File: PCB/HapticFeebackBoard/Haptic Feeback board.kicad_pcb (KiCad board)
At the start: 2 copper layers, 43.5 x 37.5 mm, 12 parts, among them J1 1769, J2 Conn_01x02, M1 Conn_01x02, M2 Conn_01x02, Q1 2N7002E, SW1 PTS526 SM15 SMTR2 LFS

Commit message: Generated Gerber Files
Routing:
- net Net-(C1-Pad1): track 6.64 -> 10.3 mm
- net GND: vias 3 -> 4
- added copper zone on B.Cu, net GND
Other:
- board size 43.5 x 37.5 mm -> 46 x 41 mm
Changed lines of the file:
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@@
 			(disableapertmacros no)
 			(usegerberextensions no)
-			(usegerberattributes yes)
+			(usegerberattributes no)
 			(usegerberadvancedattributes yes)
 			(creategerberjobfile yes)
@@
 			(outputformat 1)
 			(mirror no)
-			(drillshape 1)
+			(drillshape 0)
 			(scaleselection 1)
 			(outputdirectory "")
@@
 			(size 1.175 1.45)
 			(layers "F.Cu" "F.Paste" "F.Mask")
-			(roundrect_rratio 0.212766)
+			(roundrect_rratio 0.2127659574)
 			(net 1 "Net-(C1-Pad1)")
 			(pintype "passive")
@@
 			(size 1.175 1.45)
 			(layers "F.Cu" "F.Paste" "F.Mask")
-			(roundrect_rratio 0.212766)
+			(roundrect_rratio 0.2127659574)
 			(net 2 "GND")
 			(pintype "passive")
@@
 			(layers "*.Cu" "*.Mask")
 			(remove_unused_layers no)
-			(roundrect_rratio 0.143678)
+			(roundrect_rratio 0.1436781609)
 			(net 6 "/MCU")
 			(pinfunction "Pin_1")
@@
 			(layers "*.Cu" "*.Mask")
 			(remove_unused_layers no)
-			(roundrect_rratio 0.143678)
+			(roundrect_rratio 0.1436781609)
 			(net 5 "/Motor1")
 			(pinfunction "Pin_1")
@@
 			(layers "*.Cu" "*.Mask")
 			(remove_unused_layers no)
-			(roundrect_rratio 0.143678)
+			(roundrect_rratio 0.1436781609)
 			(net 5 "/Motor1")
 			(pinfunction "Pin_1")
@@
 			(size 1.2 1.4)
 			(layers "F.Cu" "F.Paste" "F.Mask")
-			(roundrect_rratio 0.208333)
+			(roundrect_rratio 0.2083333333)
 			(net 1 "Net-(C1-Pad1)")
 			(pintype "passive")
@@
 			(size 1.2 1.4)
 			(layers "F.Cu" "F.Paste" "F.Mask")
-			(roundrect_rratio 0.208333)
+			(roundrect_rratio 0.2083333333)
 			(net 6 "/MCU")
 			(pintype "passive")
@@
 	)
 	(gr_rect
-		(start 119.5 78.5)
-		(end 163 116)
+		(start 118.5 77)
+		(end 164.5 118)
 		(stroke
 			(width 0.1)
@@
 		(layer "Edge.Cuts")
 	)
-	(dimension
-		(type aligned)
-		(layer "F.Cu")
-		(pts
-			(xy 156.5 112) (xy 156.5 83)
-		)
-		(height 12.5)
-		(gr_text "29.0000 mm"
-			(at 167.2 97.5 90)
-			(layer "F.Cu")
-			(effects
-				(font
-					(size 1.5 1.5)
-					(thickness 0.3)
-				)
-			)
-		)
-		(format
-			(prefix "")
-			(suffix "")
-			(units 3)
-			(units_format 1)
-			(precision 4)
-		)
-		(style
-			(thickness 0.2)
-			(arrow_length 1.27)
-			(text_position_mode 0)
-			(extension_height 0.58642)
-			(extension_offset 0.5) keep_text_aligned)
-	)
-	(dimension
-		(type aligned)
+	(segment
+		(start 134.239 96.3676)
+		(end 135.9447 96.3676)
+		(width 0.254)
 		(layer "F.Cu")
-		(pts
-			(xy 156.5 112) (xy 125.5 112)
-		)
-		(height -9)
-		(gr_text "31.0000 mm"
-			(at 141 119.2 0)
-			(layer "F.Cu")
-			(effects
-				(font
-					(size 1.5 1.5)
-					(thickness 0.3)
-				)
-			)
-		)
-		(format
-			(prefix "")
-			(suffix "")
-			(units 3)
-			(units_format 1)
-			(precision 4)
-		)
-		(style
-			(thickness 0.2)
-			(arrow_length 1.27)
-			(text_position_mode 0)
-			(extension_height 0.58642)
-			(extension_offset 0.5) keep_text_aligned)
+		(net 1)
 	)
 	(segment
 		(start 134.239 96.3676)
-		(end 135.9447 96.3676)
+		(end 134.239 92.667602)
 		(width 0.254)
 		(layer "F.Cu")
@@
 	)
 	(via
-		(at 152.5 90)
+		(at 132.5 88)
+		(size 0.8)
+		(drill 0.4)
+		(layers "F.Cu" "B.Cu")
+		(free yes)
+		(net 2)
+	)
+	(via
+		(at 140.5 107.5)
 		(size 0.8)
 		(drill 0.4)
@@
 	)
 	(via
-		(at 141 108)
+		(at 141 95)
 		(size 0.8)
 		(drill 0.4)
@@
 	)
 	(via
-		(at 131.5 88)
+		(at 152 88)
 		(size 0.8)
 		(drill 0.4)
@@
 			)
 		)
+	)
+	(zone
+		(net 2)
+		(net_name "GND")
+		(layer "B.Cu")
+		(hatch edge 0.5)
+		(priority 1)
+		(connect_pads
+			(clearance 0.5)
+		)
+		(min_thickness 0.25)
+		(filled_areas_thickness no)
+		(fill yes
+			(thermal_gap 0.5)
+			(thermal_bridge_width 0.5)
+		)
+		(polygon
+			(pts
+				(xy 93.5 70) (xy 175.5 70) (xy 176 130.5) (xy 93.5 130)
+			)
+		)

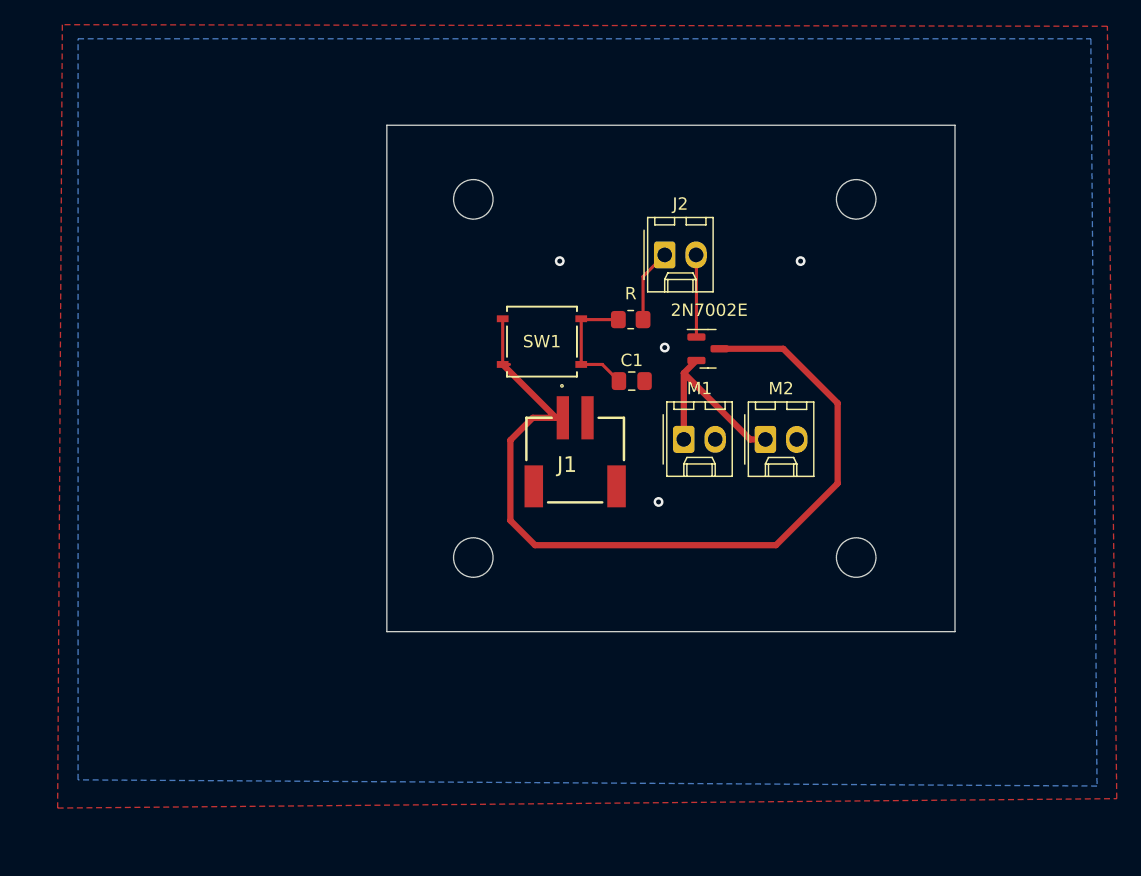
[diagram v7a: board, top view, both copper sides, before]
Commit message: Minor copper pour adjustments
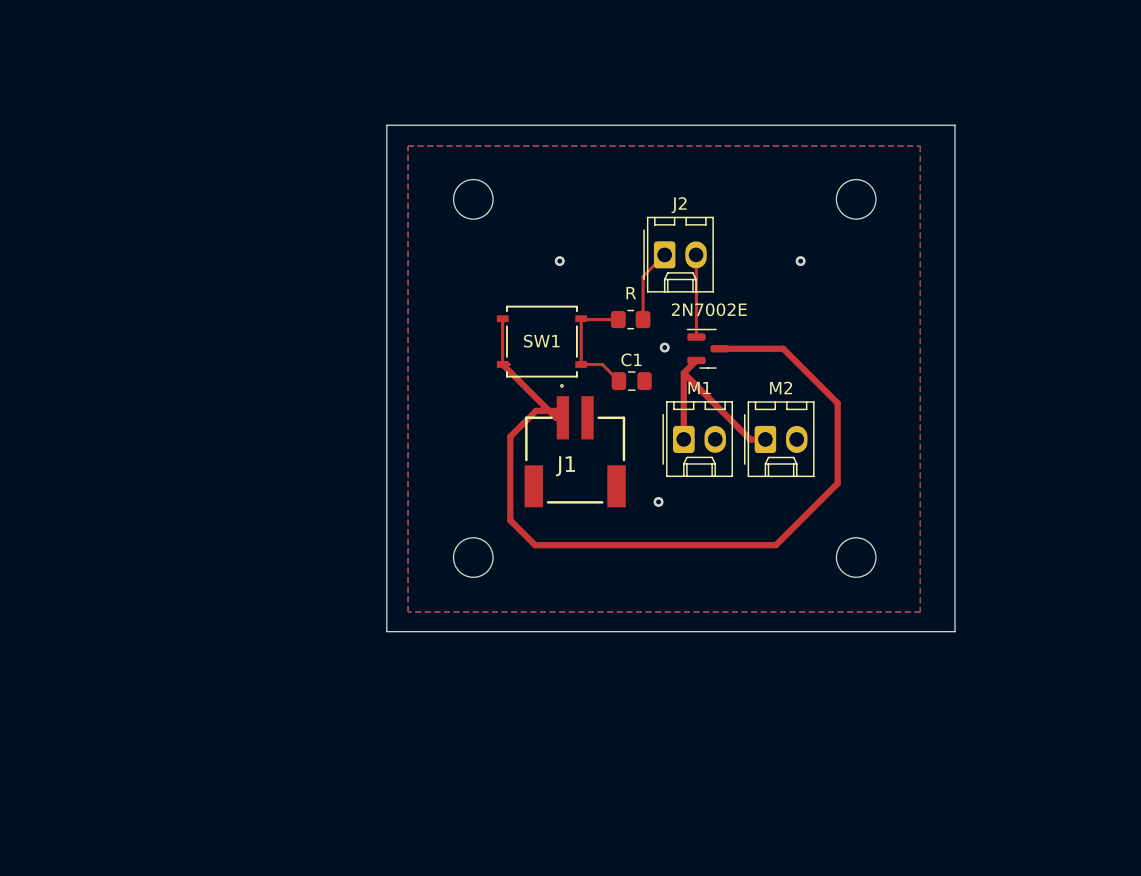
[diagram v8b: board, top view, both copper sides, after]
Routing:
- net /BMS Power: track 69.7 -> 70.3 mm
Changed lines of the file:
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@@
 		(layer "Edge.Cuts")
+	)
+	(dimension
+		(type aligned)
+		(layer "B.Cu")
+		(pts
+			(xy 118.5 77) (xy 118.5 118)
+		)
+		(height 2.4728)
+		(gr_text "1614.1732 mils"
+			(at 114.2272 97.5 90)
+			(layer "B.Cu")
+			(effects
+				(font
+					(size 1.5 1.5)
+					(thickness 0.3)
+				)
+			)
+		)
+		(format
+			(prefix "")
+			(suffix "")
+			(units 3)
+			(units_format 1)
+			(precision 4)
+		)
+		(style
+			(thickness 0.2)
+			(arrow_length 1.27)
+			(text_position_mode 0)
+			(extension_height 0.58642)
+			(extension_offset 0.5) keep_text_aligned)
+	)
+	(dimension
+		(type aligned)
+		(layer "B.Cu")
+		(pts
+			(xy 118.5 77) (xy 164.5 77)
+		)
+		(height -2.7304)
+		(gr_text "1811.0236 mils"
+			(at 141.5 72.4696 0)
+			(layer "B.Cu")
+			(effects
+				(font
+					(size 1.5 1.5)
+					(thickness 0.3)
+				)
+			)
+		)
+		(format
+			(prefix "")
+			(suffix "")
+			(units 3)
+			(units_format 1)
+			(precision 4)
+		)
+		(style
+			(thickness 0.2)
+			(arrow_length 1.27)
+			(text_position_mode 0)
+			(extension_height 0.58642)
+			(extension_offset 0.5) keep_text_aligned)
 	)
 	(segment
@@
 	)
 	(segment
-		(start 130.3144 100.6856)
-		(end 128.5 102.5)
-		(width 0.508)
-		(layer "F.Cu")
-		(net 3)
-	)
-	(segment
 		(start 132.747 100.6856)
 		(end 132.196302 100.6856)
@@
 	)
 	(segment
-		(start 128.5 102.5)
-		(end 128.5 109)
+		(start 130.5814 100.1268)
+		(end 128.5 102.2082)
 		(width 0.508)
 		(layer "F.Cu")
@@
 	)
 	(segment
-		(start 132.747 100.6856)
-		(end 130.3144 100.6856)
+		(start 155 99.5)
+		(end 150.5976 95.0976)
+		(width 0.508)
+		(layer "F.Cu")
+		(net 3)
+	)
+	(segment
+		(start 128.5 102.2082)
+		(end 128.5 109)
 		(width 0.508)
 		(layer "F.Cu")
@@
 	)
 	(segment
+		(start 155 106)
+		(end 155 99.5)
+		(width 0.508)
+		(layer "F.Cu")
+		(net 3)
+	)
+	(segment
+		(start 132.1882 100.1268)
+		(end 130.5814 100.1268)
+		(width 0.508)
+		(layer "F.Cu")
+		(net 3)
+	)
+	(segment
+		(start 127.878302 96.3676)
+		(end 127.878302 92.667602)
+		(width 0.25)
+		(layer "F.Cu")
+		(net 3)
+	)
+	(segment
+		(start 150 111)
+		(end 155 106)
+		(width 0.508)
+		(layer "F.Cu")
+		(net 3)
+	)
+	(segment
+		(start 132.196302 100.6856)
+		(end 127.878302 96.3676)
+		(width 0.508)
+		(layer "F.Cu")
+		(net 3)
+	)
+	(segment
+		(start 130.5 111)
+		(end 150 111)
+		(width 0.508)
+		(layer "F.Cu")
+		(net 3)
+	)
+	(segment
+		(start 132.747 100.6856)
+		(end 132.1882 100.1268)
+		(width 0.508)
+		(layer "F.Cu")
+		(net 3)
+	)
+	(segment
 		(start 128.5 109)
 		(end 130.5 111)
-		(width 0.508)
-		(layer "F.Cu")
-		(net 3)
-	)
-	(segment
-		(start 155 99.5)
-		(end 150.5976 95.0976)
-		(width 0.508)
-		(layer "F.Cu")
-		(net 3)
-	)
-	(segment
-		(start 150 111)
-		(end 155 106)
-		(width 0.508)
-		(layer "F.Cu")
-		(net 3)
-	)
-	(segment
-		(start 127.878302 96.3676)
-		(end 127.878302 92.667602)
-		(width 0.25)
-		(layer "F.Cu")
-		(net 3)
-	)
-	(segment
-		(start 130.5 111)
-		(end 150 111)
-		(width 0.508)
-		(layer "F.Cu")
-		(net 3)
-	)
-	(segment
-		(start 132.196302 100.6856)
-		(end 127.878302 96.3676)
-		(width 0.508)
-		(layer "F.Cu")
-		(net 3)
-	)
-	(segment
-		(start 155 106)
-		(end 155 99.5)
 		(width 0.508)
 		(layer "F.Cu")
@@
 		(polygon
 			(pts
-				(xy 176.8348 68.9864) (xy 92.2274 68.8594) (xy 91.8464 132.2832) (xy 177.5968 131.5212)
+				(xy 120.2182 78.6892) (xy 161.6964 78.6892) (xy 161.6964 116.4082) (xy 120.2182 116.4082)
 			)
 		)
@@
 		(layer "B.Cu")
 		(hatch edge 0.5)
-		(priority 1)
 		(connect_pads
 			(clearance 0.5)
@@
 		(polygon
 			(pts
-				(xy 93.5 70) (xy 175.5 70) (xy 176 130.5) (xy 93.5 130)
+				(xy 120.2182 78.6892) (xy 161.6964 78.6892) (xy 161.6964 116.4082) (xy 120.2182 116.4082)
 			)
 		)
